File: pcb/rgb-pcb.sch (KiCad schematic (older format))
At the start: 19 parts

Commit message: Added RS232 to schematic
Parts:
- removed J?: SER-POW_IN, symbol SER-POW_IN
- added C? (x2): 0.1uF, symbol C
- added C? (x3): 0.47uF, symbol C
- added IC?: MAX3232, symbol MAX3232
- added J?: SERIAL-POWER_out, symbol 8P8C_CUSTOM
- added J?: SERIAL-POWER_in, symbol 8P8C_CUSTOM
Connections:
- net labels added: RS_RX, RS_TX
- wire segments 155 -> 197
- no-connect marks 3 -> 5

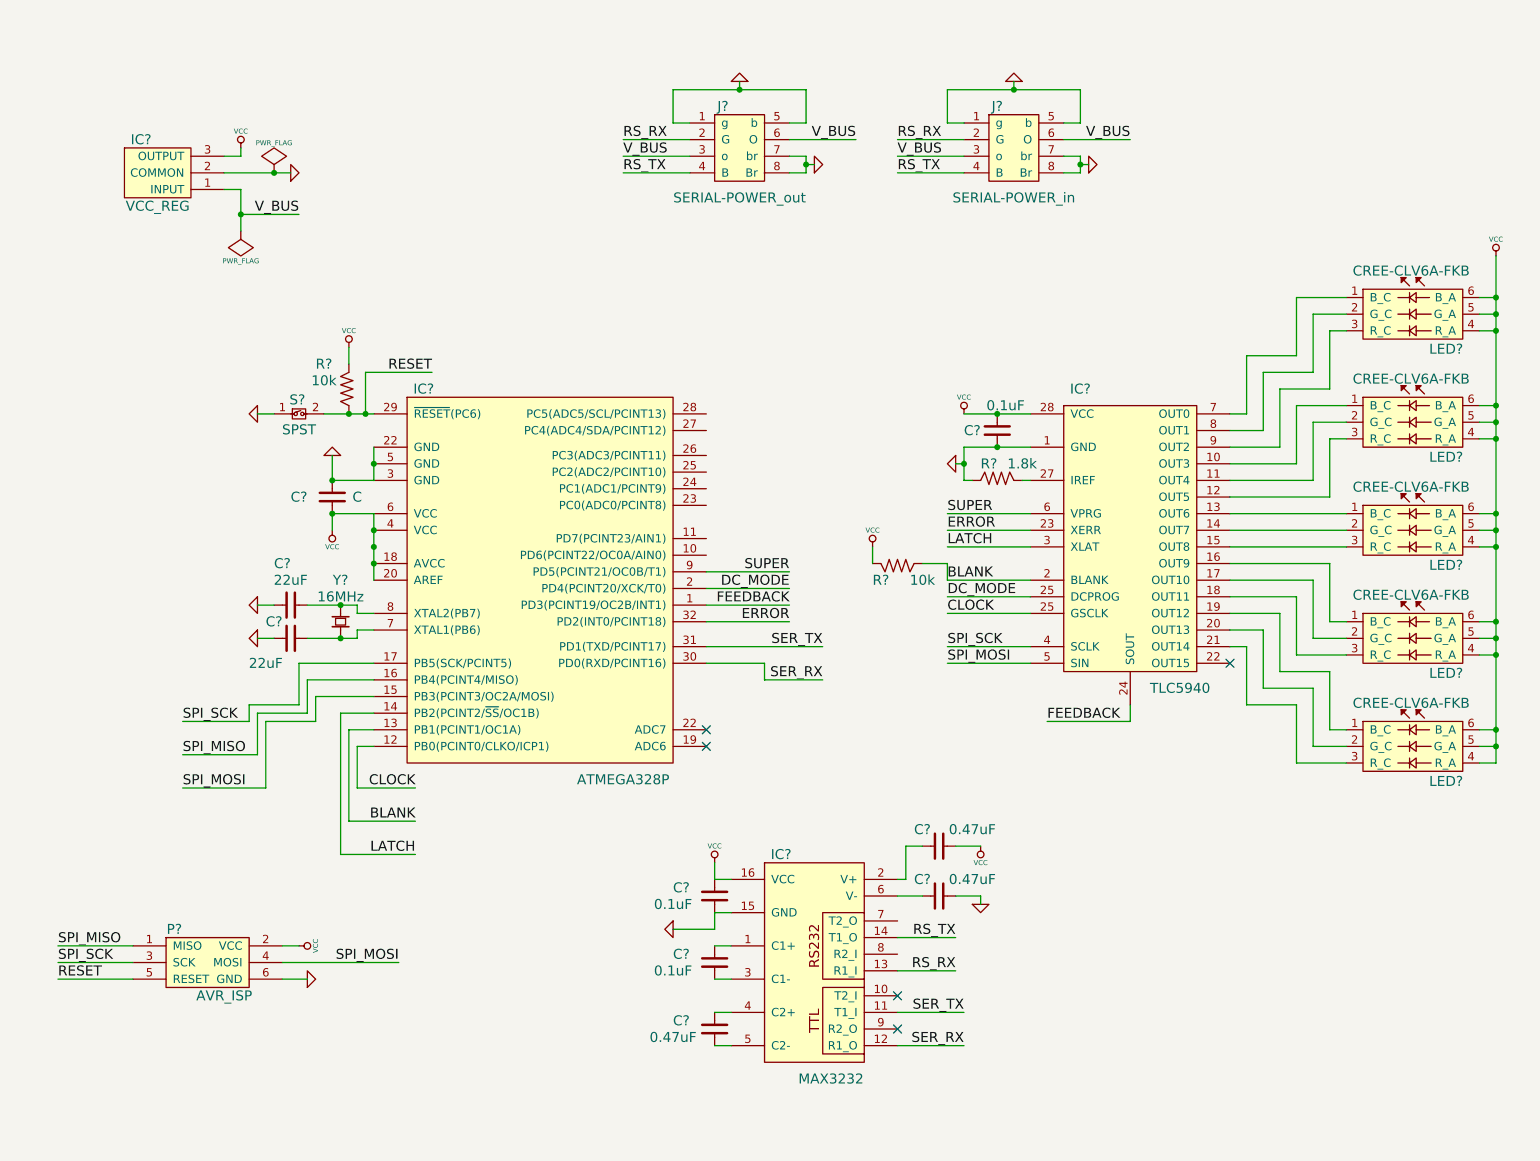
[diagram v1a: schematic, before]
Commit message: Initial schematic seems finished. Might need to add some debugging pins
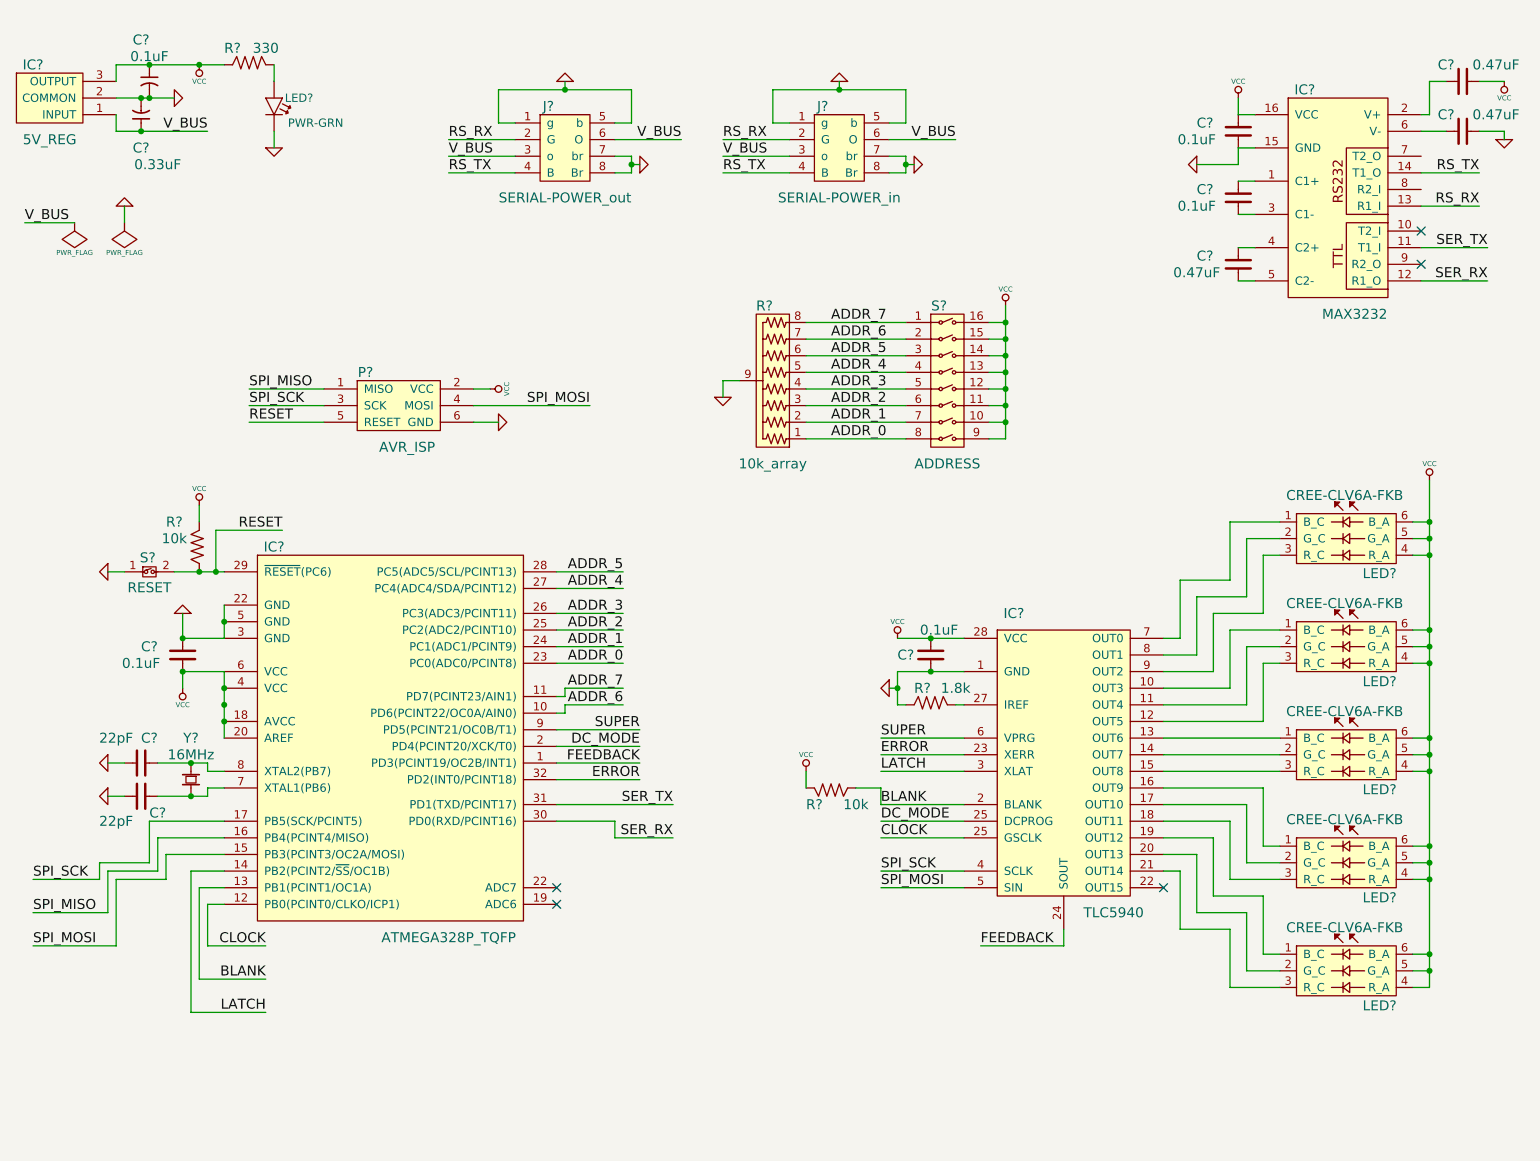
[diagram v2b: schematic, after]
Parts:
- added C?: 0.33uF, symbol C_POL
- added C?: 0.1uF, symbol C_POL
- added LED?: PWR-GRN, symbol LED
- added R?: 10k_array, symbol R-ARRAY_X8-BUSSED
- added R?: 330, symbol R
- added S?: ADDRESS, symbol SPST_X8
- C?: value C -> 0.1uF
- C? (x2): value 22uF -> 22pF
- IC?: value ATMEGA328P -> ATMEGA328P_TQFP
- IC?: value VCC_REG -> 5V_REG
- S?: value SPST -> RESET
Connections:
- net GND: now also C?.2, C?.2, LED?.2 (K), R?.9 (COMMON)
- net VCC: now also C?.1, R?.1, S?.10, S?.11, S?.12, S?.13, S?.14, S?.15, S?.16, S?.9
- net V_BUS: now also C?.1
- net ADDR_6: now reaches IC?.10 (PD6(PCINT22/OC0A/AIN0))
- net ADDR_6: now also R?.7 (R7), S?.2
- net ADDR_7: now reaches IC?.11 (PD7(PCINT23/AIN1))
- net ADDR_7: now also R?.8 (R8), S?.1
- net ADDR_0: now reaches IC?.23 (PC0(ADC0/PCINT8))
- net ADDR_0: now also R?.1 (R1), S?.8
- net ADDR_1: now reaches IC?.24 (PC1(ADC1/PCINT9))
- net ADDR_1: now also R?.2 (R2), S?.7
- net ADDR_2: now reaches IC?.25 (PC2(ADC2/PCINT10))
- net ADDR_2: now also R?.3 (R3), S?.6
- net ADDR_3: now reaches IC?.26 (PC3(ADC3/PCINT11))
- net ADDR_3: now also R?.4 (R4), S?.5
- net ADDR_4: now reaches IC?.27 (PC4(ADC4/SDA/PCINT12))
- net ADDR_4: now also R?.5 (R5), S?.4
- net ADDR_5: now reaches IC?.28 (PC5(ADC5/SCL/PCINT13))
- net ADDR_5: now also R?.6 (R6), S?.3
- new net: LED?.1 (A), R?.2
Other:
- moved on the sheet: C?, IC?, J?, LED?, P?, R?, S?, Y?

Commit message: Added that debugging header and improved the power circuits
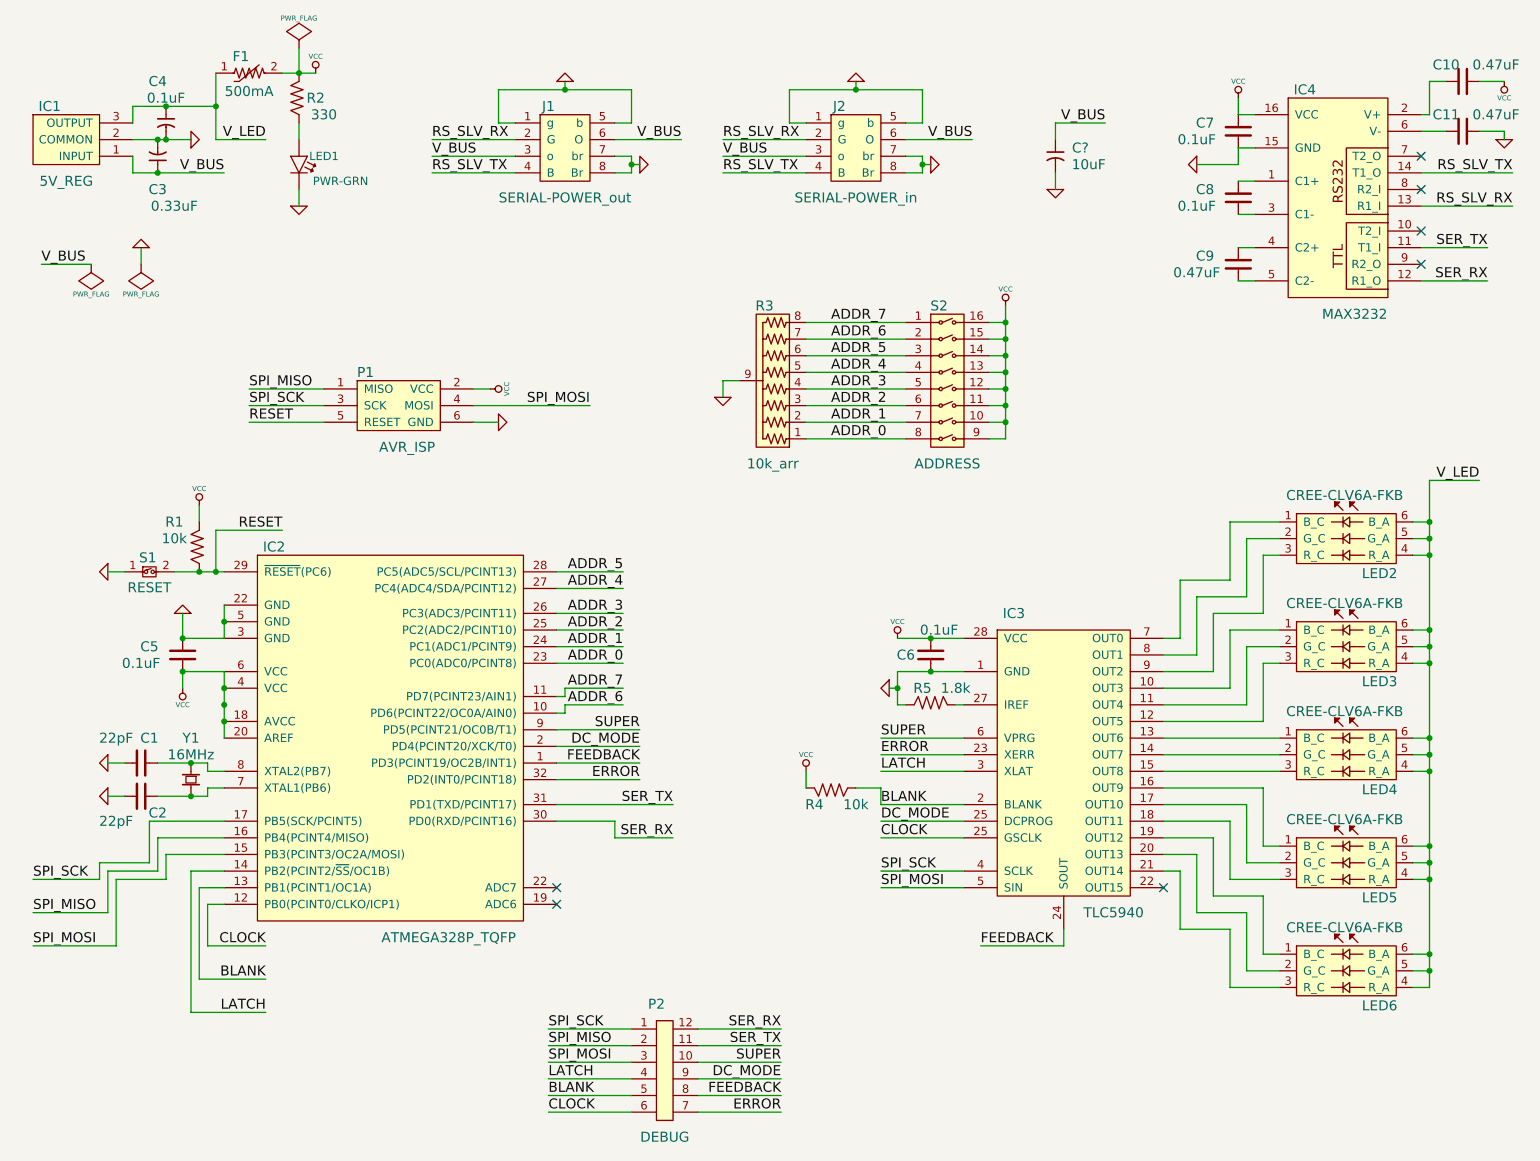
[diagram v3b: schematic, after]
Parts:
- added C?: 10uF, symbol C_POL
- added F1: 500mA, symbol PTC
- added P2: DEBUG, symbol 12PIN_HEADER
- R3: renamed from R?; value 10k_array -> 10k_arr
- gave numbers to parts that had none: 31
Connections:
- net BLANK: now also P2.5
- net CLOCK: now also P2.6
- net DC_MODE: now also P2.9
- net ERROR: now also P2.7
- net FEEDBACK: now also P2.8
- net GND: now also C?.2
- net LATCH: now also P2.4
- net SER_RX: now also P2.12
- net SER_TX: now also P2.11
- net SPI_MISO: now also P2.2
- net SPI_MOSI: now also P2.3
- net SPI_SCK: now also P2.1
- net SUPER: now also P2.10
- net VCC: now also R2.2, F1.2; no longer C4.1, IC1.3 (OUTPUT), LED2.4 (R_A), LED2.5 (G_A), LED2.6 (B_A), LED3.4 (R_A), LED3.5 (G_A), LED3.6 (B_A), LED4.4 (R_A), LED4.5 (G_A), LED4.6 (B_A), LED5.4 (R_A), LED5.5 (G_A), LED5.6 (B_A), LED6.4 (R_A), LED6.5 (G_A), LED6.6 (B_A), R2.1
- net V_BUS: now also C?.1
- net at LED1.1 (A): now also R2.1; no longer R2.2
- net RS_RX renamed RS_SLV_RX
- net RS_TX renamed RS_SLV_TX
- new net V_LED: C4.1, F1.1, IC1.3 (OUTPUT), LED2.4 (R_A), LED2.5 (G_A), LED2.6 (B_A), LED3.4 (R_A), LED3.5 (G_A), LED3.6 (B_A), LED4.4 (R_A), LED4.5 (G_A), LED4.6 (B_A), LED5.4 (R_A), LED5.5 (G_A), LED5.6 (B_A), LED6.4 (R_A), LED6.5 (G_A), LED6.6 (B_A)
- no-connect marks 5 -> 7
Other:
- moved on the sheet: C3, C4, IC1, J2, LED1, R2

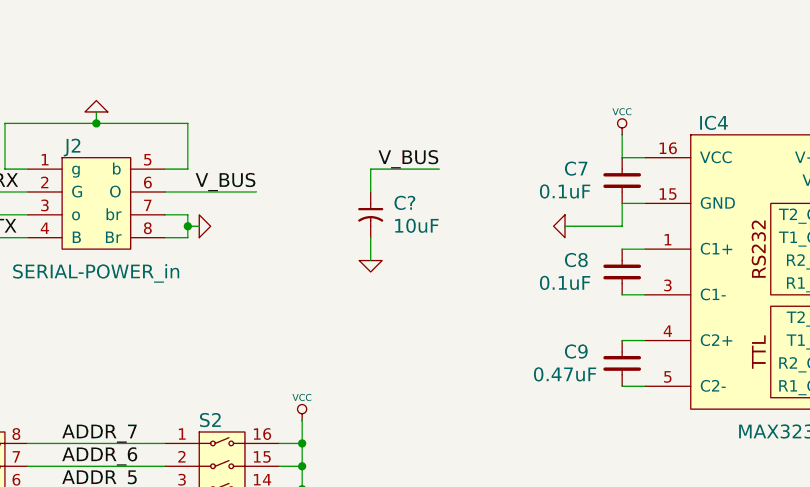
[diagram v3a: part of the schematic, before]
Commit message: Moving on to component package selection
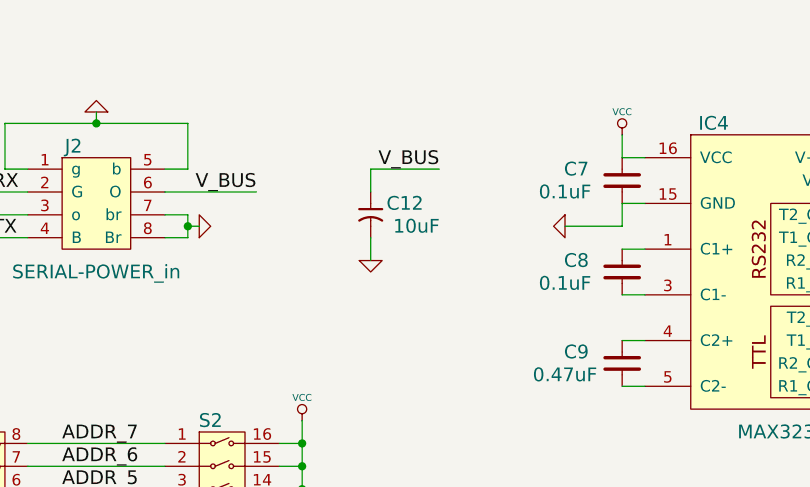
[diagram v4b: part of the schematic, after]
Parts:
- gave numbers to parts that had none: 1
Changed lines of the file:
@@
-EESchema Schematic File Version 2  date Sat 04 May 2013 07:07:01 PM CDT
+EESchema Schematic File Version 2  date Sat 04 May 2013 07:19:22 PM CDT
 LIBS:standard
 LIBS:avr-mcu
@@
 	7350 1750 7350 1650
 $Comp
-L GND #PWR?
+L GND #PWR01
 U 1 1 5185A1C4
 P 7350 1750
-F 0 "#PWR?" H 7350 1750 30  0001 C CNN
+F 0 "#PWR01" H 7350 1750 30  0001 C CNN
 F 1 "GND" H 7350 1680 30  0001 C CNN
 	1    7350 1750
@@
 V_BUS
 $Comp
-L C_POL C?
+L C_POL C12
 U 1 1 5185A18C
 P 7350 1550
-F 0 "C?" V 7300 1700 60  0000 C CNN
+F 0 "C12" V 7300 1700 60  0000 C CNN
 F 1 "10uF" V 7400 1750 60  0000 C CNN
 	1    7350 1550
@@
 $EndComp
 $Comp
-L PWR_FLAG #FLG01
+L PWR_FLAG #FLG02
 U 1 1 5185A0FC
 P 2800 900
-F 0 "#FLG01" H 2800 995 30  0001 C CNN
+F 0 "#FLG02" H 2800 995 30  0001 C CNN
 F 1 "PWR_FLAG" H 2800 1080 30  0000 C CNN
 	1    2800 900
@@
 NoConn ~ 9550 1550
 $Comp
-L GND #PWR02
+L GND #PWR03
 U 1 1 518598E3
 P 2800 1850
-F 0 "#PWR02" H 2800 1850 30  0001 C CNN
+F 0 "#PWR03" H 2800 1850 30  0001 C CNN
 F 1 "GND" H 2800 1780 30  0001 C CNN
 	1    2800 1850
@@
 $EndComp
 $Comp
-L GND #PWR03
+L GND #PWR04
 U 1 1 51859848
 P 1850 2100
-F 0 "#PWR03" H 1850 2100 30  0001 C CNN
+F 0 "#PWR04" H 1850 2100 30  0001 C CNN
 F 1 "GND" H 1850 2030 30  0001 C CNN
 	1    1850 2100
@@
 V_BUS
 $Comp
-L GND #PWR04
+L GND #PWR05
 U 1 1 51859815
 P 2150 1450
-F 0 "#PWR04" H 2150 1450 30  0001 C CNN
+F 0 "#PWR05" H 2150 1450 30  0001 C CNN
 F 1 "GND" H 2150 1380 30  0001 C CNN
 	1    2150 1450
@@
 $EndComp
 $Comp
-L VCC #PWR05
+L VCC #PWR06
 U 1 1 51859808
 P 2900 1050
-F 0 "#PWR05" H 2900 1150 30  0001 C CNN
+F 0 "#PWR06" H 2900 1150 30  0001 C CNN
 F 1 "VCC" H 2900 1150 30  0000 C CNN
 	1    2900 1050
@@
 $EndComp
 $Comp
-L GND #PWR06
+L GND #PWR07
 U 1 1 5185945E
 P 5350 3000
-F 0 "#PWR06" H 5350 3000 30  0001 C CNN
+F 0 "#PWR07" H 5350 3000 30  0001 C CNN
 F 1 "GND" H 5350 2930 30  0001 C CNN
 	1    5350 3000
@@
 ADDR_0
 $Comp
-L VCC #PWR07
+L VCC #PWR08
 U 1 1 518593DD
 P 7050 2450
-F 0 "#PWR07" H 7050 2550 30  0001 C CNN
+F 0 "#PWR08" H 7050 2550 30  0001 C CNN
 F 1 "VCC" H 7050 2550 30  0000 C CNN
 	1    7050 2450
@@
 NoConn ~ 9550 2000
 $Comp
-L GND #PWR08
+L GND #PWR09
 U 1 1 51858766
 P 10050 1450
-F 0 "#PWR08" H 10050 1450 30  0001 C CNN
+F 0 "#PWR09" H 10050 1450 30  0001 C CNN
 F 1 "GND" H 10050 1380 30  0001 C CNN
 	1    10050 1450
@@
 $EndComp
 $Comp
-L VCC #PWR09
+L VCC #PWR010
 U 1 1 5185875E
 P 10050 1100
-F 0 "#PWR09" H 10050 1200 30  0001 C CNN
+F 0 "#PWR010" H 10050 1200 30  0001 C CNN
 F 1 "VCC" H 10050 1200 30  0000 C CNN
 	1    10050 1100
@@
 $EndComp
 $Comp
-L VCC #PWR010
+L VCC #PWR011
 U 1 1 5185873E
 P 8450 1200
-F 0 "#PWR010" H 8450 1300 30  0001 C CNN
+F 0 "#PWR011" H 8450 1300 30  0001 C CNN
 F 1 "VCC" H 8450 1300 30  0000 C CNN
 	1    8450 1200
@@
 $EndComp
 $Comp
-L GND #PWR011
+L GND #PWR012
 U 1 1 51858708
 P 8200 1600
-F 0 "#PWR011" H 8200 1600 30  0001 C CNN
+F 0 "#PWR012" H 8200 1600 30  0001 C CNN
 F 1 "GND" H 8200 1530 30  0001 C CNN
 	1    8200 1600
@@
 RS_SLV_RX
 $Comp
-L GND #PWR012
+L GND #PWR013
 U 1 1 51858011
 P 6600 1600
-F 0 "#PWR012" H 6600 1600 30  0001 C CNN
+F 0 "#PWR013" H 6600 1600 30  0001 C CNN
 F 1 "GND" H 6600 1530 30  0001 C CNN
 	1    6600 1600
@@
 V_BUS
 $Comp
-L GND #PWR013
+L GND #PWR014
 U 1 1 51858010
 P 6150 1100
-F 0 "#PWR013" H 6150 1100 30  0001 C CNN
+F 0 "#PWR014" H 6150 1100 30  0001 C CNN
 F 1 "GND" H 6150 1030 30  0001 C CNN
 	1    6150 1100
@@
 $EndComp
 $Comp
-L PWR_FLAG #FLG014
+L PWR_FLAG #FLG015
 U 1 1 51857FF0
 P 1550 2200
-F 0 "#FLG014" H 1550 2295 30  0001 C CNN
+F 0 "#FLG015" H 1550 2295 30  0001 C CNN
 F 1 "PWR_FLAG" H 1550 2380 30  0000 C CNN
 	1    1550 2200
@@
 $EndComp
 $Comp
-L PWR_FLAG #FLG015
+L PWR_FLAG #FLG016
 U 1 1 51857FD3
 P 1850 2200
-F 0 "#FLG015" H 1850 2295 30  0001 C CNN
+F 0 "#FLG016" H 1850 2295 30  0001 C CNN
 F 1 "PWR_FLAG" H 1850 2380 30  0000 C CNN
 	1    1850 2200
@@
 $EndComp
 $Comp
-L GND #PWR016
+L GND #PWR017
 U 1 1 51857FA6
 P 4400 1100
-F 0 "#PWR016" H 4400 1100 30  0001 C CNN
+F 0 "#PWR017" H 4400 1100 30  0001 C CNN
 F 1 "GND" H 4400 1030 30  0001 C CNN
 	1    4400 1100
@@
 V_BUS
 $Comp
-L GND #PWR017
+L GND #PWR018
 U 1 1 51857F67
 P 4850 1600
-F 0 "#PWR017" H 4850 1600 30  0001 C CNN
+F 0 "#PWR018" H 4850 1600 30  0001 C CNN
 F 1 "GND" H 4850 1530 30  0001 C CNN
 	1    4850 1600
@@
 DC_MODE
 $Comp
-L VCC #PWR018
+L VCC #PWR019
 U 1 1 5181F756
 P 5850 5250
-F 0 "#PWR018" H 5850 5350 30  0001 C CNN
+F 0 "#PWR019" H 5850 5350 30  0001 C CNN
 F 1 "VCC" H 5850 5350 30  0000 C CNN
 	1    5850 5250
@@
 SPI_MOSI
 $Comp
-L GND #PWR019
+L GND #PWR020
 U 1 1 5181EFE1
 P 4000 3150
-F 0 "#PWR019" H 4000 3150 30  0001 C CNN
+F 0 "#PWR020" H 4000 3150 30  0001 C CNN
 F 1 "GND" H 4000 3080 30  0001 C CNN
 	1    4000 3150
@@
 $EndComp
 $Comp
-L VCC #PWR020
+L VCC #PWR021
 U 1 1 5181EFDA
 P 3950 2950
-F 0 "#PWR020" H 3950 3050 30  0001 C CNN
+F 0 "#PWR021" H 3950 3050 30  0001 C CNN
 F 1 "VCC" H 3950 3050 30  0000 C CNN
 	1    3950 2950
@@
 $EndComp
 $Comp
-L GND #PWR021
+L GND #PWR022
 U 1 1 5181EFA2
 P 1650 4050
-F 0 "#PWR021" H 1650 4050 30  0001 C CNN
+F 0 "#PWR022" H 1650 4050 30  0001 C CNN
 F 1 "GND" H 1650 3980 30  0001 C CNN
 	1    1650 4050
@@
 $EndComp
 $Comp
-L VCC #PWR022
+L VCC #PWR023
 U 1 1 5181EF92
 P 2200 3650
-F 0 "#PWR022" H 2200 3750 30  0001 C CNN
+F 0 "#PWR023" H 2200 3750 30  0001 C CNN
 F 1 "VCC" H 2200 3750 30  0000 C CNN
 	1    2200 3650
@@
 $EndComp
 $Comp
-L GND #PWR023
+L GND #PWR024
 U 1 1 5181B718
 P 1650 5400
-F 0 "#PWR023" H 1650 5400 30  0001 C CNN
+F 0 "#PWR024" H 1650 5400 30  0001 C CNN
 F 1 "GND" H 1650 5330 30  0001 C CNN
 	1    1650 5400
@@
 $EndComp
 $Comp
-L GND #PWR024
+L GND #PWR025
 U 1 1 5181B714
 P 1650 5200
-F 0 "#PWR024" H 1650 5200 30  0001 C CNN
+F 0 "#PWR025" H 1650 5200 30  0001 C CNN
 F 1 "GND" H 1650 5130 30  0001 C CNN
 	1    1650 5200
@@
 $EndComp
 $Comp
-L GND #PWR025
+L GND #PWR026
 U 1 1 5181B47A
 P 2100 4300
-F 0 "#PWR025" H 2100 4300 30  0001 C CNN
+F 0 "#PWR026" H 2100 4300 30  0001 C CNN
 F 1 "GND" H 2100 4230 30  0001 C CNN
 	1    2100 4300
@@
 $EndComp
 $Comp
-L VCC #PWR026
+L VCC #PWR027
 U 1 1 5181B46F
 P 2100 4750
-F 0 "#PWR026" H 2100 4850 30  0001 C CNN
+F 0 "#PWR027" H 2100 4850 30  0001 C CNN
 F 1 "VCC" H 2100 4850 30  0000 C CNN
 	1    2100 4750
@@
 $EndComp
 $Comp
-L GND #PWR027
+L GND #PWR028
 U 1 1 5181AC1B
 P 6350 4750
-F 0 "#PWR027" H 6350 4750 30  0001 C CNN
+F 0 "#PWR028" H 6350 4750 30  0001 C CNN
 F 1 "GND" H 6350 4680 30  0001 C CNN
 	1    6350 4750
@@
 $EndComp
 $Comp
-L VCC #PWR028
+L VCC #PWR029
 U 1 1 5181AC0E
 P 6400 4450
-F 0 "#PWR028" H 6400 4550 30  0001 C CNN
+F 0 "#PWR029" H 6400 4550 30  0001 C CNN
 F 1 "VCC" H 6400 4550 30  0000 C CNN
 	1    6400 4450
